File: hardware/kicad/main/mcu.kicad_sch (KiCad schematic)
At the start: 16 parts, among them J10 SWD, U10 MDBT50Q-U1MV2, U11 W25Q128JVSIQ, Y1 32.768k 9pF

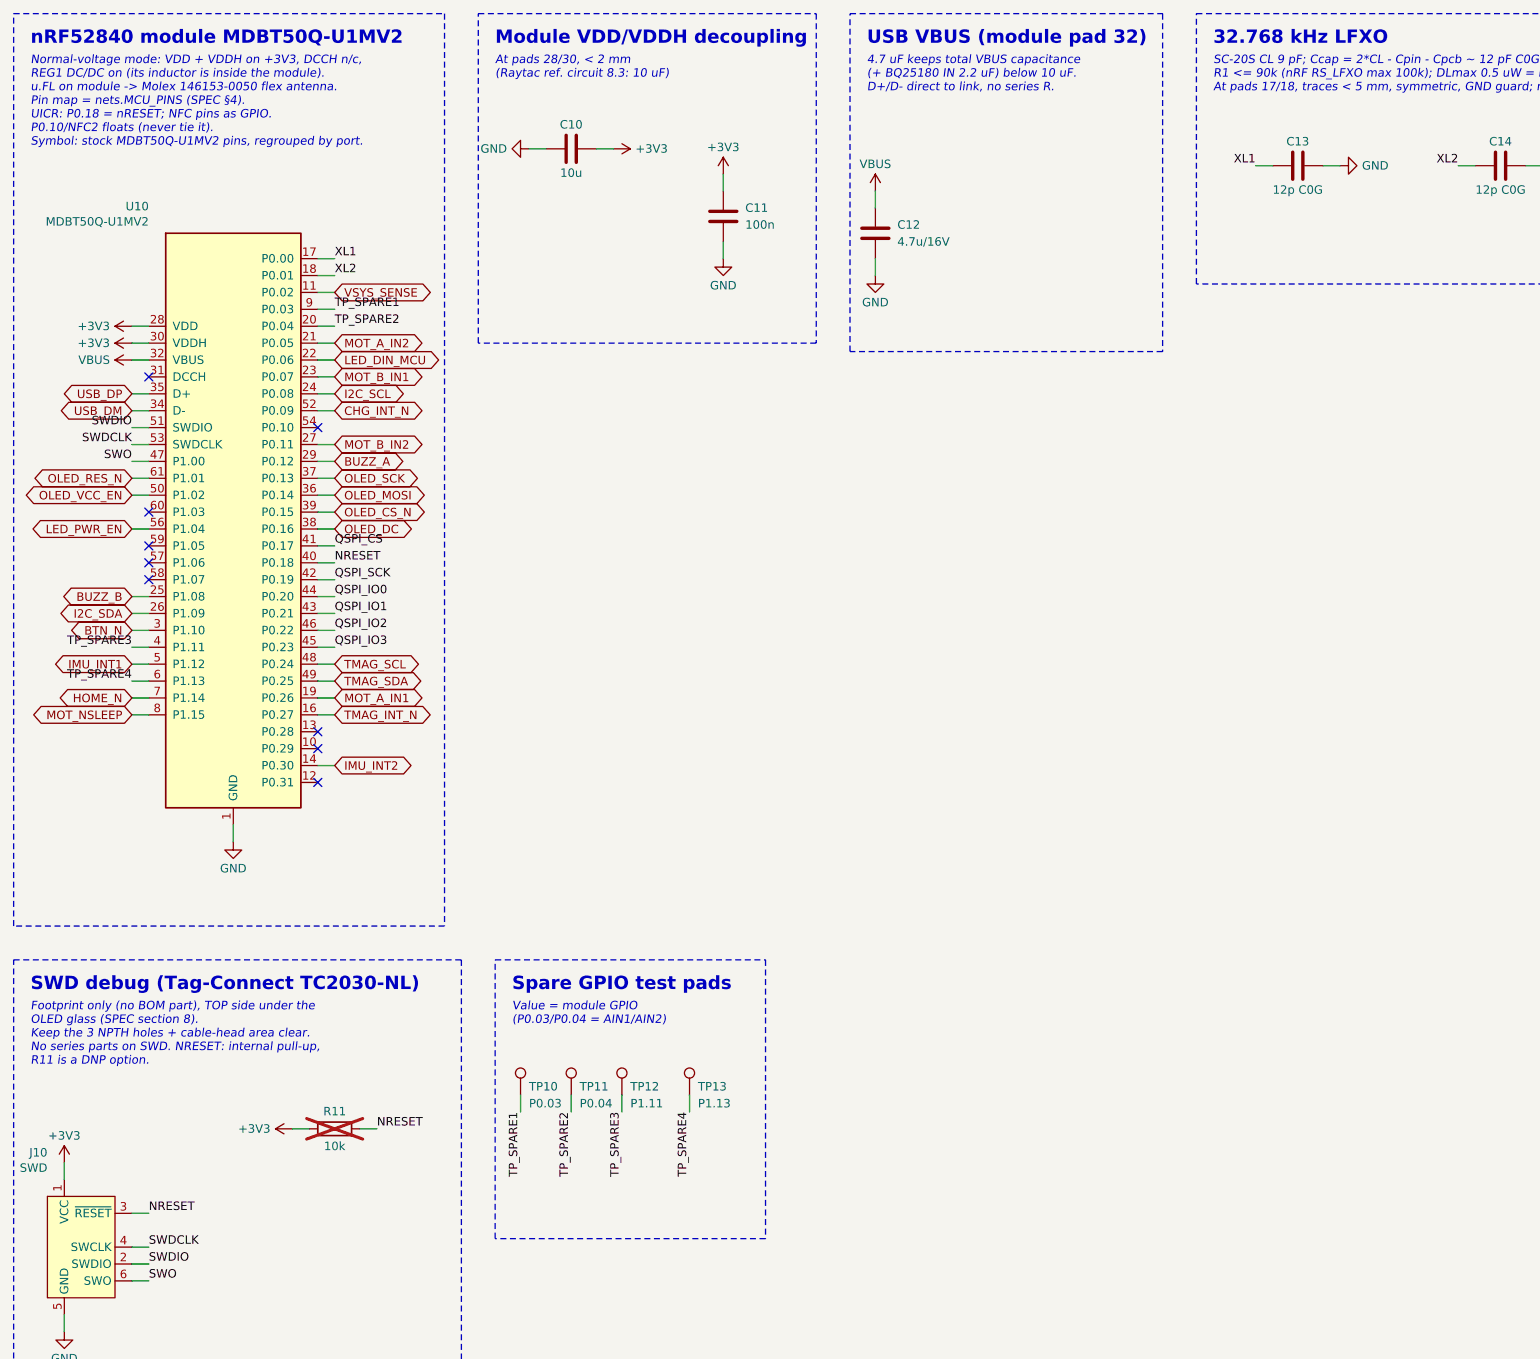
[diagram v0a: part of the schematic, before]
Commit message: NFC tag: P0.09/P0.10 as NFC1/NFC2 with 180 pF tuning caps and coil pads; CHG_INT_N moves to P1.03
Co-Authored-By: Claude Opus 5.5 <noreply@anthropic.com>
Claude-Session: https://claude.ai/code/session_01P3cqdBhxLcWY3sGUVf9LAJ
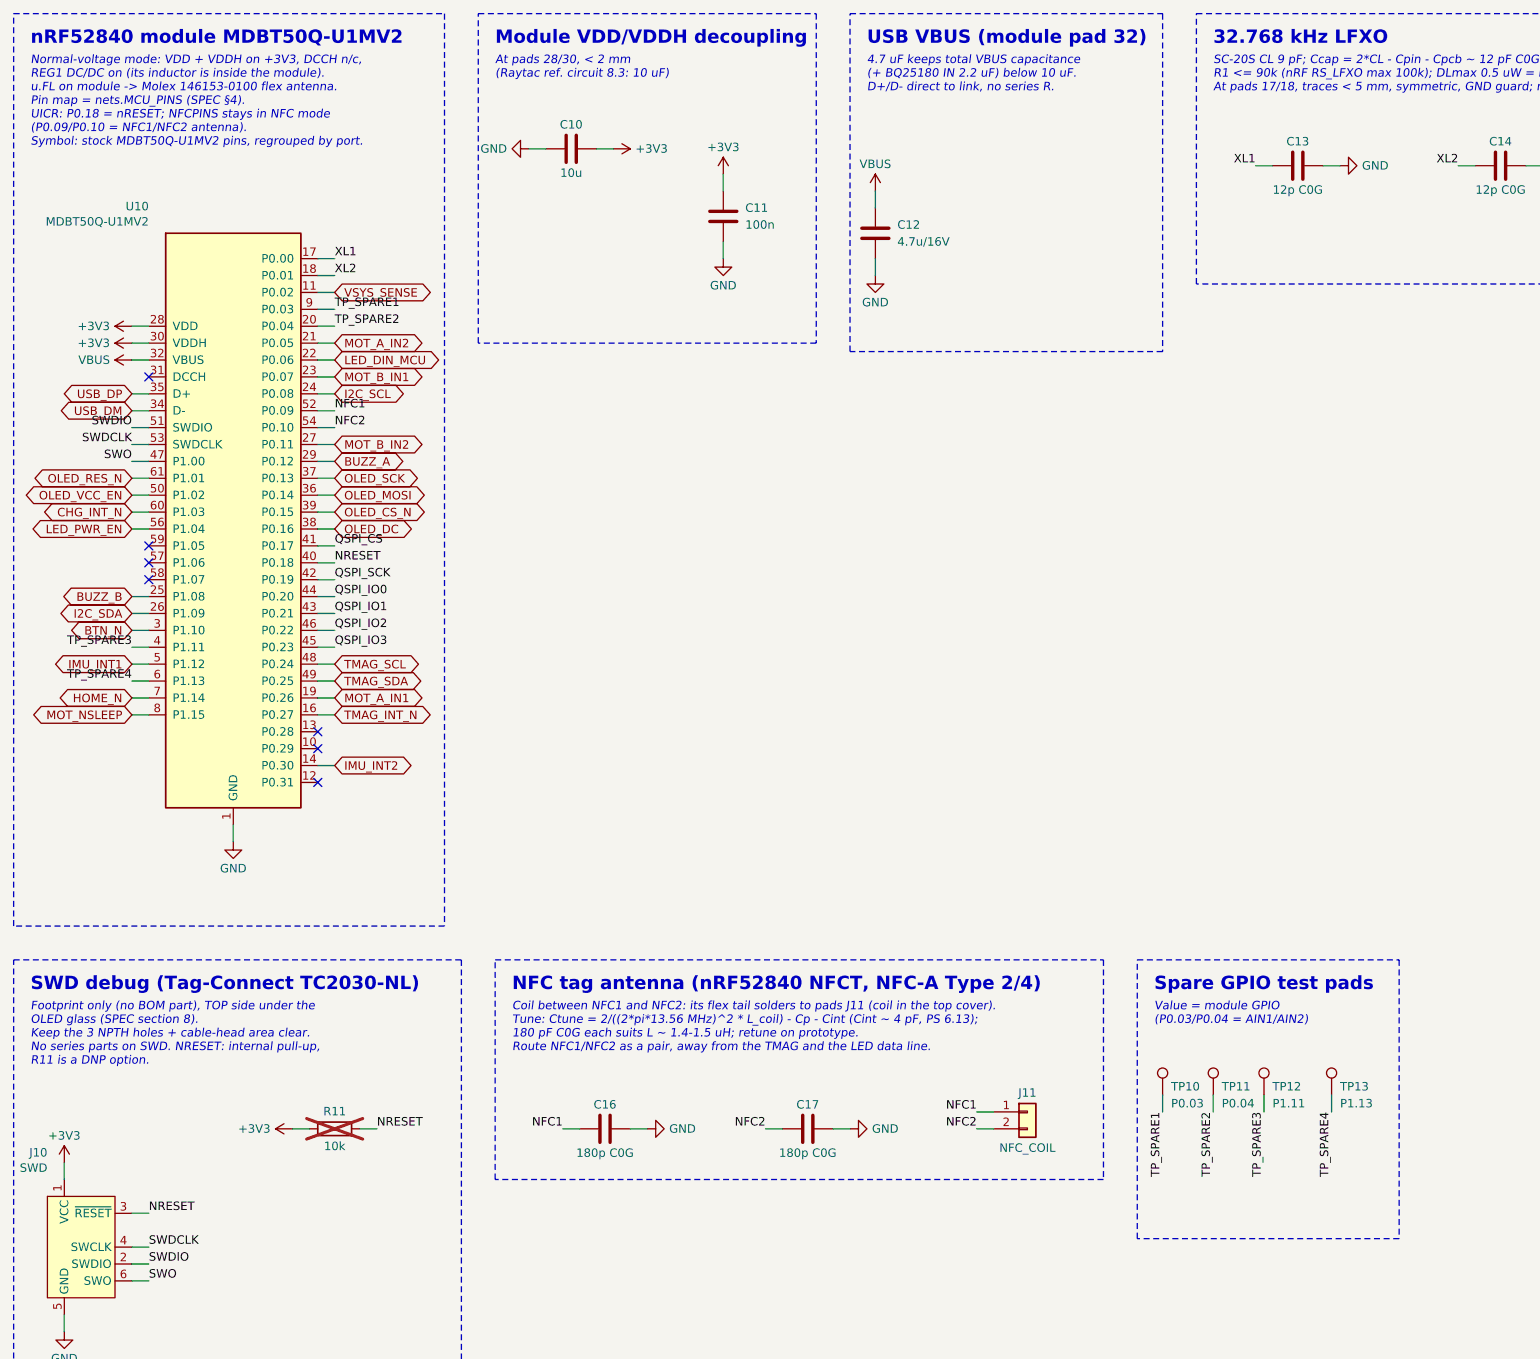
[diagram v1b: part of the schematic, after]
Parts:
- added C16, C17: 180p C0G, Capacitor_SMD:C_0402_1005Metric, symbol Device:C
- added J11: NFC_COIL, dial_spinner:NFC_Coil_Pads_1x02_P2.0mm, symbol Connector_Generic:Conn_01x02
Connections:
- net CHG_INT_N: now also U10.60 (P1.03); no longer U10.52 (P0.09)
- net GND: now also C16.2, C17.2
- net NFC2: now reaches U10.54 (P0.10)
- net NFC2: now also C17.1, J11.2 (Pin_2)
- new net NFC1: C16.1, J11.1 (Pin_1), U10.52 (P0.09)
- no-connect marks 9 -> 7
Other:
- note added: "Coil between NFC1 and NFC2: its flex tail solders to pads J11 (coil in the top cover). Tune: Ctune = 2/((2*pi*13.56 MHz)^2 * L_coil) - Cp - Cint (Cint ~ 4 pF, PS 6.13); 180 pF C0G each suits L ~ 1.4-1.5 uH; retune on prototype. Route NFC1/NFC2 as a pair, away from the TMAG and the LED data line."
- note added: "NFC tag antenna (nRF52840 NFCT, NFC-A Type 2/4)"
- note added: "Normal-voltage mode: VDD + VDDH on +3V3, DCCH n/c, REG1 DC/DC on (its inductor is inside the module). u.FL on module -> Molex 146153-0100 flex antenna. Pin map = nets.MCU_PINS (SPEC §4). UICR: P0.18 = nRESET; NFCPINS stays in NFC mode (P0.09/P0.10 = NFC1/NFC2 antenna). Symbol: stock MDBT50Q-U1MV2 pins, regrouped by port."
- note removed: "Normal-voltage mode: VDD + VDDH on +3V3, DCCH n/c, REG1 DC/DC on (its inductor is inside the module). u.FL on module -> Molex 146153-0050 flex antenna. Pin map = nets.MCU_PINS (SPEC §4). UICR: P0.18 = nRESET; NFC pins as GPIO. P0.10/NFC2 floats (never tie it). Symbol: stock MDBT50Q-U1MV2 pins, regrouped by port."
- moved on the sheet: TP10, TP11, TP12, TP13

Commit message: Main schematic: ERC clean (VBUS_NRF power flag, documented waiver for U21 QOD tied to VOUT); Freerouting pass cap; load-switch test numerics fallback
- build.py: ERC_WAIVERS lists intended pin-type violations; waived ones are reported as such, never dropped
- mcu.py: PWR_FLAG on VBUS_NRF (fed from VBUS through R12)
- display.py: L20 note gives Isat 0.72 A rated (0.92 A typical)
- layout.py: also pass --router.max_passes (Freerouting 2.1 ignores -mp)
- test_load_switches.py: run() retries stalled/hung decks with looser numerics (verifier NEW-6)

Co-Authored-By: Claude Opus 5.5 <noreply@anthropic.com>
Claude-Session: https://claude.ai/code/session_01P3cqdBhxLcWY3sGUVf9LAJ
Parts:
- added R12: 4.7, Resistor_SMD:R_0402_1005Metric, symbol Device:R
- added U12: USBLC6-2SC6, Package_TO_SOT_SMD:SOT-23-6, symbol Power_Protection:USBLC6-2SC6
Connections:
- net GND: now also U12.2 (GND)
- net USB_DM: now also U12.3 (I/O2), U12.4 (I/O2)
- net USB_DP: now also U12.1 (I/O1), U12.6 (I/O1)
- net VBUS: now also R12.1; no longer C12.1, U10.32 (VBUS)
- new net VBUS_NRF: C12.1, R12.2, U10.32 (VBUS), U12.5 (VBUS)
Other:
- note added: "R12 in series (nRF52840 PS 7.3 config 1): a legacy-cable hot plug rings the link VBUS to 6.5-8.4 V, above the 5.8 V VBUS abs max; with 4.7 R (Nordic's value) it peaks at 5.07-5.48 V (hardware/sim test_usb_input). DC drop ~11 mV at the 2.4 mA VBUS current. C12 on the module side; total sink C < 10 uF. U12 USBLC6 at the module: IEC 8 kV on D+/D- otherwise drives 2.6-3.7 A into the nRF pads through 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"
- note added: "USB VBUS (module pad 32) and second-stage USB ESD"
- note removed: "4.7 uF keeps total VBUS capacitance (+ BQ25180 IN 2.2 uF) below 10 uF. D+/D- direct to link, no series R."
- note removed: "USB VBUS (module pad 32)"
- moved on the sheet: C12, C13, C14, C15, C16, C17, J10, J11, R10, R11, TP10, TP11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

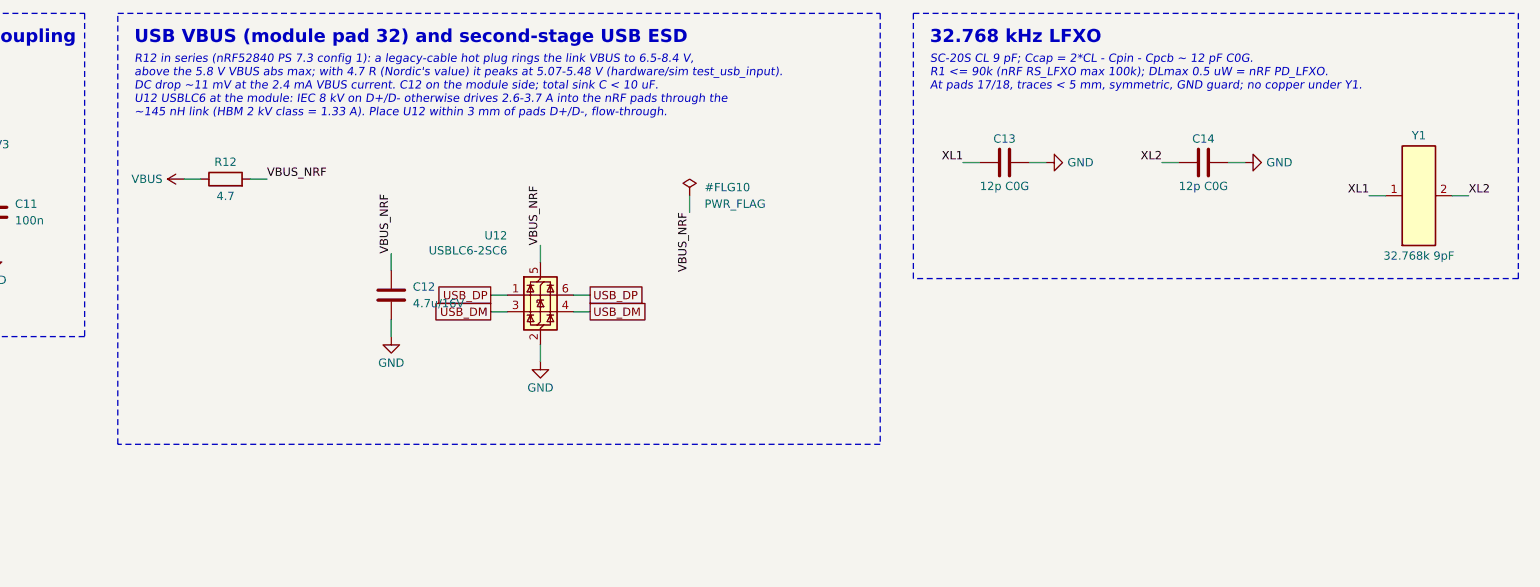
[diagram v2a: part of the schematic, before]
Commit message: Schematic notes: J1 at r 19.5, VLED fall 24/26.6 ms, hot-plug 4.49-5.49 V, SM04B J2, 100k press pull-down, SYS_REG 4.4 V, side-entry J3, LED data path and margins
Notes only; netlists unchanged. Base board still DRC-clean with schematic parity.

Co-Authored-By: Claude Opus 5.5 <noreply@anthropic.com>
Claude-Session: https://claude.ai/code/session_01P3cqdBhxLcWY3sGUVf9LAJ
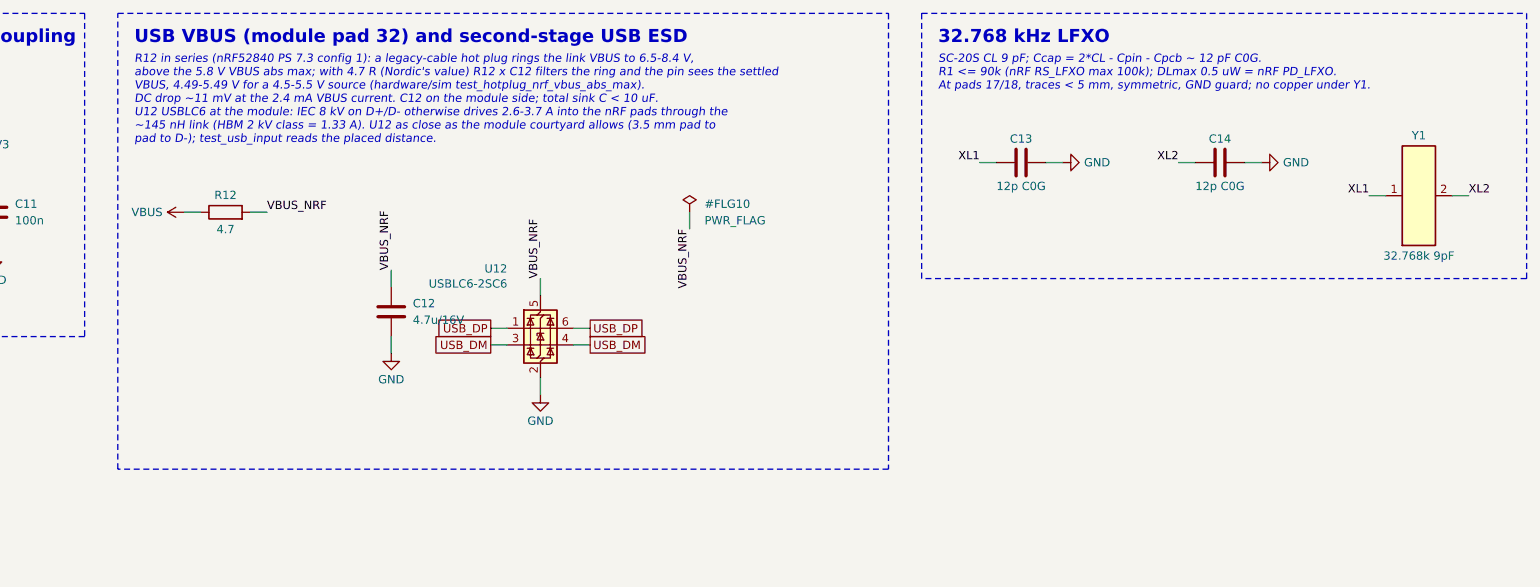
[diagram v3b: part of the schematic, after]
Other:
- note added: "R12 in series (nRF52840 PS 7.3 config 1): a legacy-cable hot plug rings the link VBUS to 6.5-8.4 V, above the 5.8 V VBUS abs max; with 4.7 R (Nordic's value) R12 x C12 filters the ring and the pin sees the settled VBUS, 4.49-5.49 V for a 4.5-5.5 V source (hardware/sim test_hotplug_nrf_vbus_abs_max). DC drop ~11 mV at the 2.4 mA VBUS current. C12 on the module side; total sink C < 10 uF. U12 USBLC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"
- note removed: "R12 in series (nRF52840 PS 7.3 config 1): a legacy-cable hot plug rings the link VBUS to 6.5-8.4 V, above the 5.8 V VBUS abs max; with 4.7 R (Nordic's value) it peaks at 5.07-5.48 V (hardware/sim test_usb_input). DC drop ~11 mV at the 2.4 mA VBUS current. C12 on the module side; total sink C < 10 uF. U12 USBLC6 at the module: IEC 8 kV on D+/D- otherwise drives 2.6-3.7 A into the nRF pads through 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"
- moved on the sheet: C12, C13, C14, R12, U12
